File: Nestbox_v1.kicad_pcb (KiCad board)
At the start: 2 copper layers, 23 x 90 mm, 79 parts, among them P1 RX/TX, P2 TST/RST, P3 VDD/GND, P4 NFC_PWR_SEL, Q1 SFH 3605, SW1 SMD-BUTTON_2P-3.0X2.5X1.2+0.4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, U1 MSP430FR5969, U2 CR95HF, U3 TPS630250RNC, U4 RN2483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

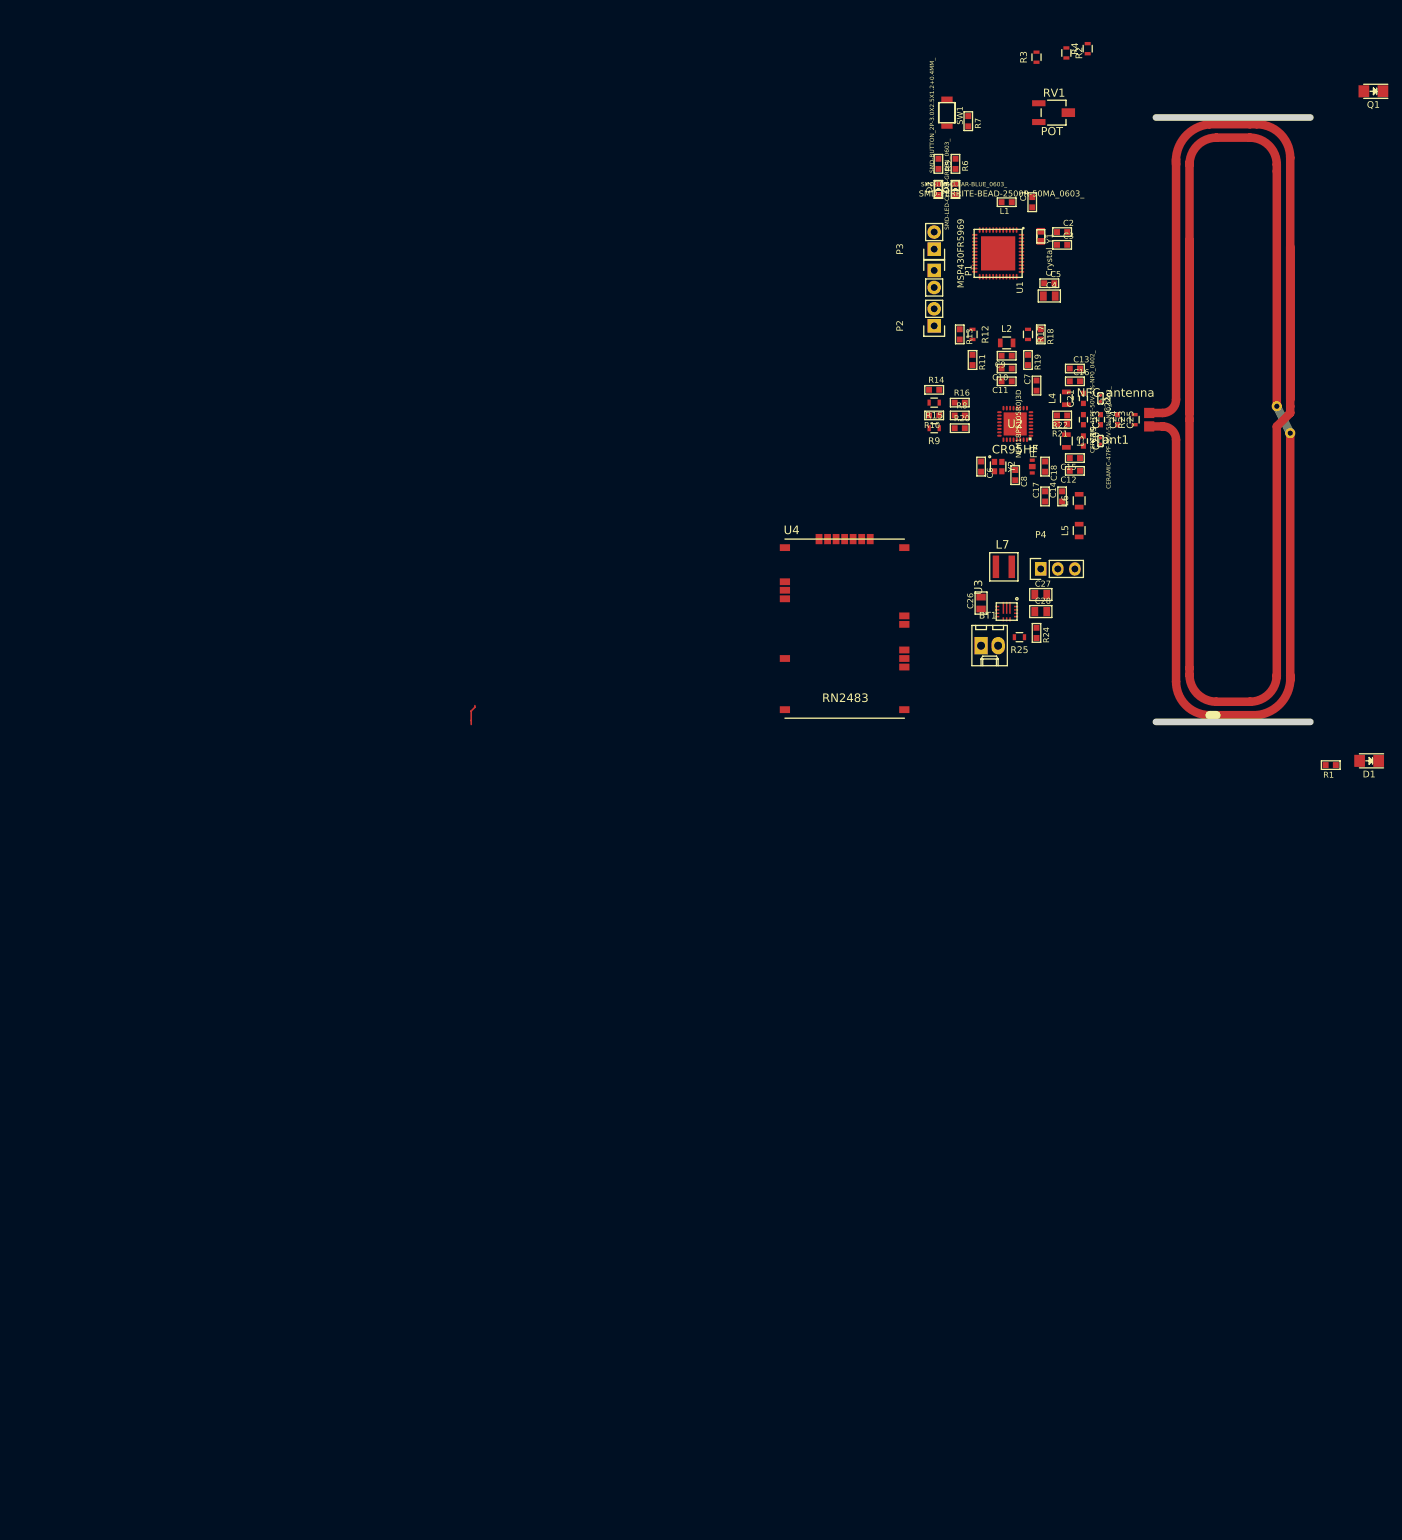
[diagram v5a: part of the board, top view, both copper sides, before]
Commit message: finished component placement incl. LoRa
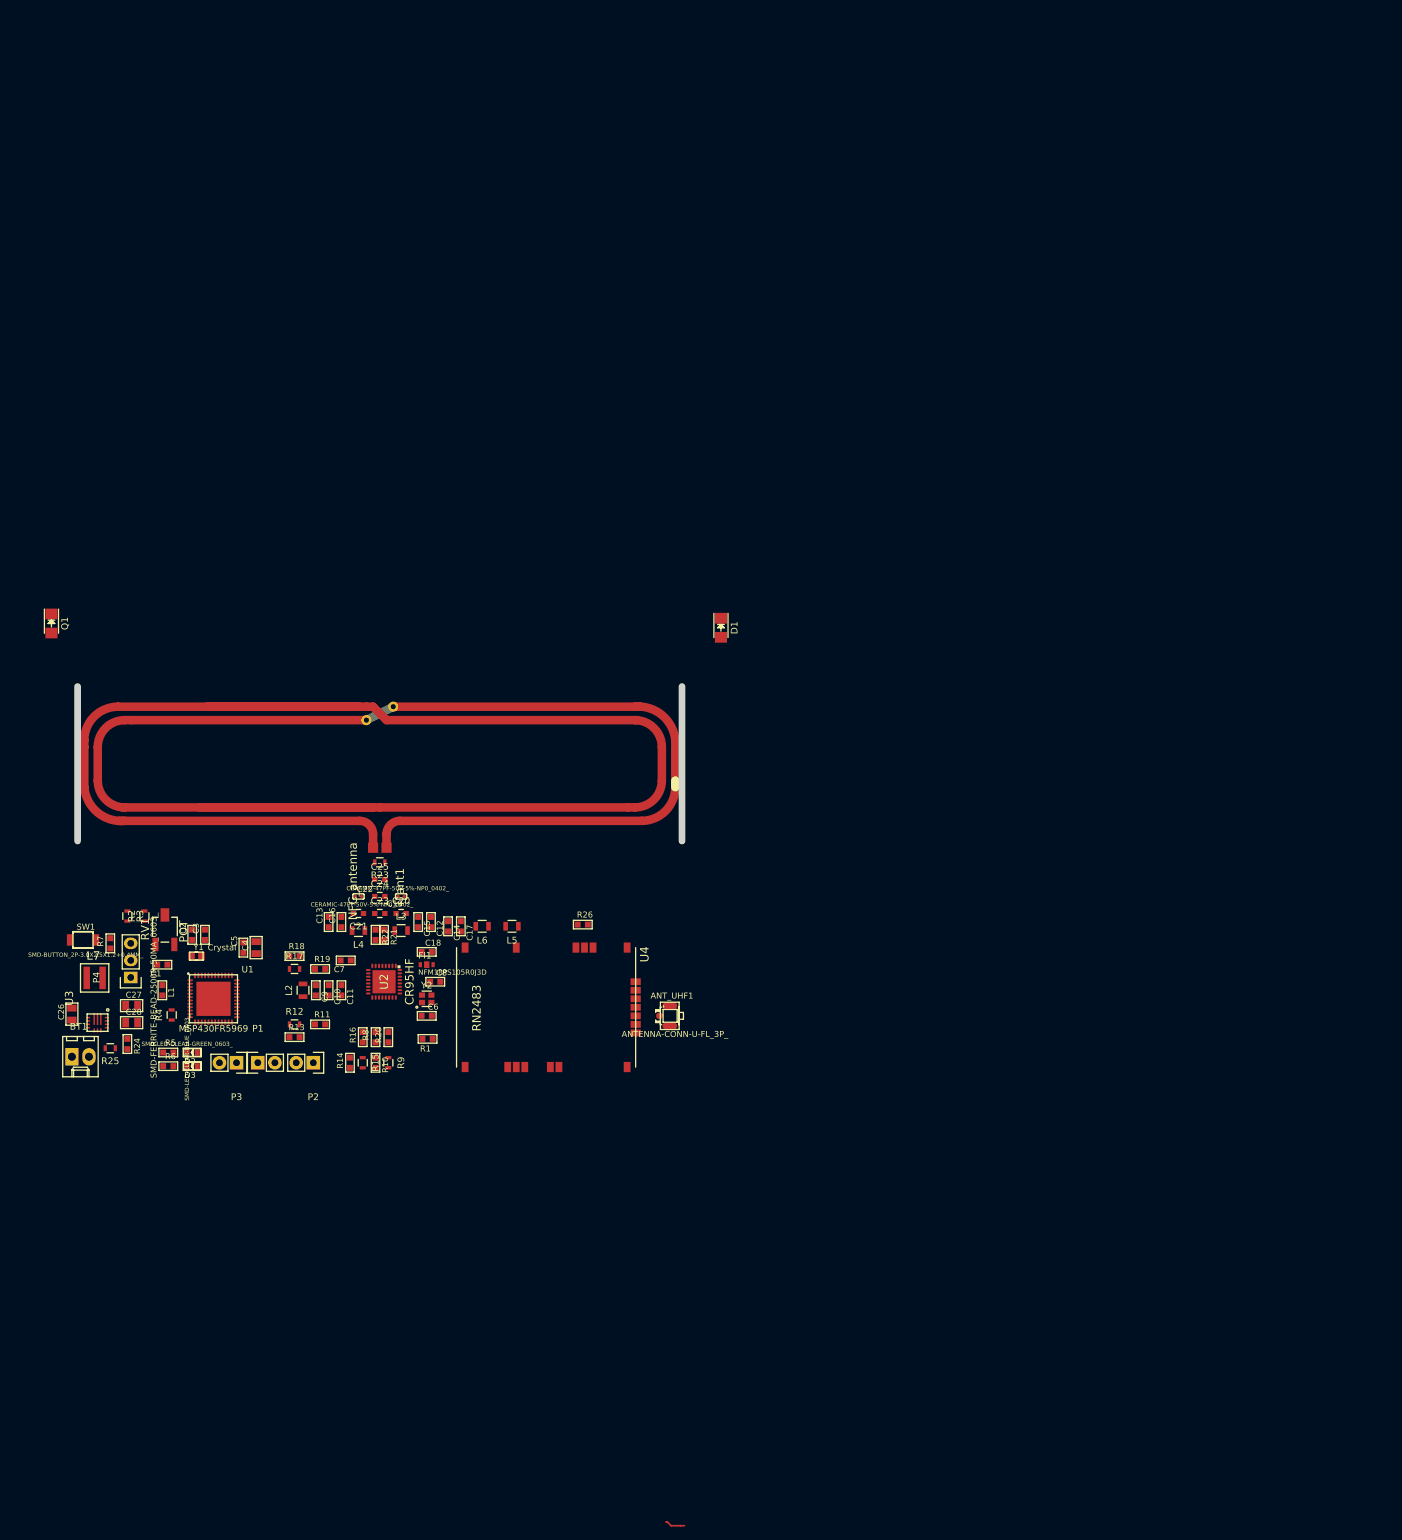
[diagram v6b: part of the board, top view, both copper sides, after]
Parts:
- added ANT_UHF1: ANTENNA-CONN-U-FL_3P_, SeeedOPL-Connector-2016:U-FL3P-SMD-2.6X2.6X1.0MM, F.Cu at (170.0, 120.9)
- added R26: SMD-RES-10K-1%-1_10W_0603_, SeeedOPL-Resistor-2016:R0603, F.Cu at (157.1, 107.4)
- moved Q1 212.2 mm to (77.9, 62.5), turned to 270 degrees
- moved R4 198.3 mm to (95.9, 120.8)
- moved R2 188.1 mm to (91.8, 106.1), turned to 90 degrees
- moved R3 186.2 mm to (89.2, 106.1), turned to 270 degrees
- moved RV1 179.8 mm to (94.8, 108.1), turned to 90 degrees
- moved R6 178.3 mm to (95.3, 128.4), turned to 270 degrees
- moved SW1 178.1 mm to (82.6, 109.6), turned to 0 degrees
- moved R7 177.0 mm to (86.7, 110.1), turned to 0 degrees
- moved R5 175.1 mm to (95.3, 126.4), turned to 270 degrees
- moved D3 173.1 mm to (98.9, 128.4), turned to 180 degrees
- moved C1 172.3 mm to (94.5, 113.3), turned to 270 degrees
- moved L1 172.0 mm to (94.5, 117.1), turned to 270 degrees
- moved D2 169.9 mm to (98.9, 126.4), turned to 180 degrees
- moved C2 166.5 mm to (98.9, 108.9), turned to 180 degrees
- moved Y1 165.2 mm to (99.5, 112.1), turned to 0 degrees
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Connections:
- U1 pad 12: (no net) -> Net-(U1-Pad12)
- U1 pad 13: (no net) -> Net-(U1-Pad13)
- U1 pad 14: (no net) -> Net-(U1-Pad14)
- U1 pad 15: (no net) -> Net-(U1-Pad15)
- U1 pad 19: (no net) -> Net-(U1-Pad19)
- U1 pad 2: (no net) -> Net-(U1-Pad2)
- U1 pad 28: (no net) -> Net-(U1-Pad28)
- U1 pad 3: (no net) -> Net-(U1-Pad3)
- U1 pad 33: (no net) -> Net-(U1-Pad33)
- U1 pad 34: (no net) -> Net-(U1-Pad34)
- U1 pad 35: (no net) -> LORA_RST_N
- U1 pad 38: (no net) -> Net-(U1-Pad38)
- U1 pad 39: (no net) -> Net-(U1-Pad39)
- U1 pad 4: (no net) -> Net-(U1-Pad4)
- U1 pad 40: (no net) -> Net-(U1-Pad40)
- U1 pad 42: (no net) -> Net-(U1-Pad42)
- U1 pad 43: (no net) -> Net-(U1-Pad43)
- U1 pad 5: (no net) -> Net-(U1-Pad5)
- U1 pad 6: (no net) -> Net-(U1-Pad6)
- U1 pad 7: (no net) -> Net-(U1-Pad7)
- U1 pad 8: (no net) -> Net-(U1-Pad8)
- U1 pad 9: (no net) -> Net-(U1-Pad9)
- U4 pad 23: (no net) -> Net-(ANT_UHF1-PadD)
- U4 pad 25: (no net) -> Net-(U4-Pad25)
- U4 pad 32: (no net) -> LORA_RST_N
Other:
- board size 23 x 90 mm -> 90 x 23 mm

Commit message: board outline
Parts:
- moved ANT_UHF1 24.3 mm to (190.8, 133.5)
- moved R26 24.0 mm to (177.4, 120.1)
- moved U4 23.5 mm to (158.3, 123.1)
- moved C14 23.4 mm to (157.3, 119.3)
- moved C17 23.4 mm to (159.2, 119.3)
- moved L5 23.4 mm to (166.8, 119.3)
- moved L6 23.4 mm to (162.4, 119.3)
- moved BT1 22.6 mm to (100.8, 138.0)
- moved C10 22.6 mm to (139.0, 128.1)
- moved C11 22.6 mm to (140.9, 128.1)
- moved C6 22.6 mm to (153.6, 131.9)
- moved C9 22.6 mm to (137.1, 128.1)
- moved FI1 22.6 mm to (153.6, 124.2)
- moved L2 22.6 mm to (135.2, 128.1)
- moved L3 22.6 mm to (149.8, 119.2)
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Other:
- board size 90 x 23 mm -> 100 x 91 mm

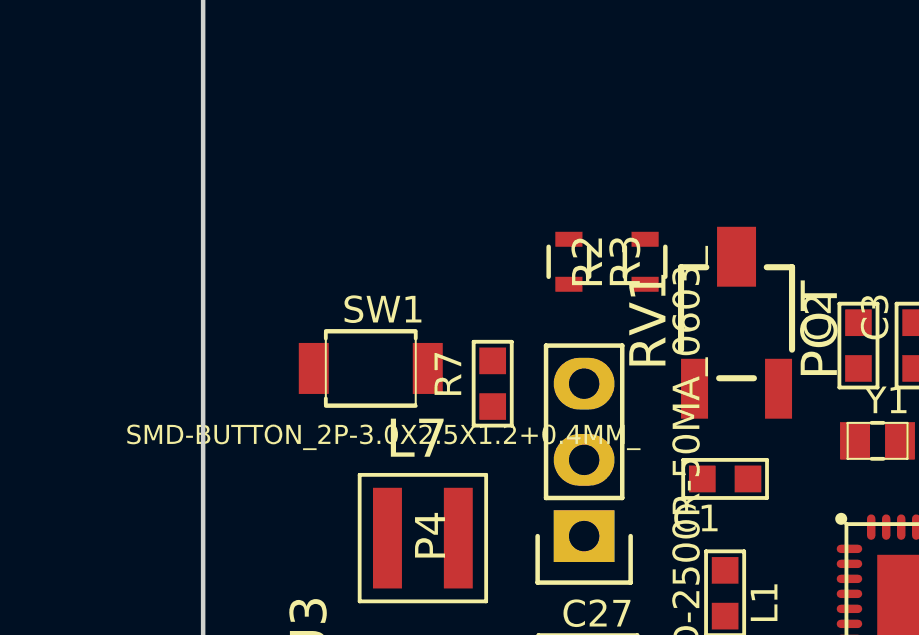
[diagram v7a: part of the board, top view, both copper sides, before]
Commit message: added additional connector for light barrier
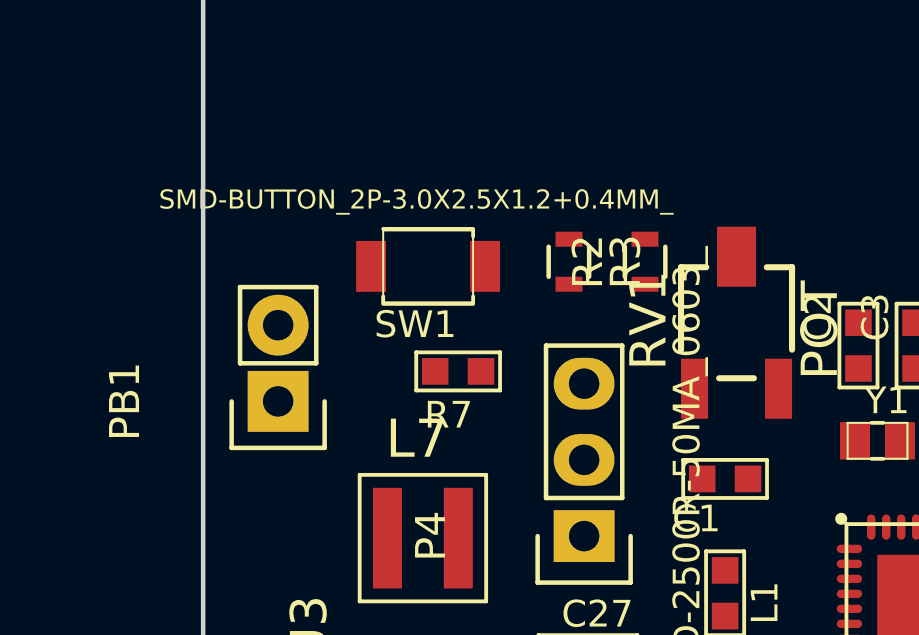
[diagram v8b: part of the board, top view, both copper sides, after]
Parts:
- added PB1: LIGHT_BARRIER2, Socket_Strips:Socket_Strip_Straight_1x02, F.Cu at (99.4, 121.7)
- moved SW1 3.90 mm to (104.4, 117.2), turned to 180 degrees
- moved R7 1.22 mm to (105.4, 120.7), turned to 90 degrees
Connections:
- U1 pad 12: Net-(U1-Pad12) -> (no net)
- U1 pad 13: Net-(U1-Pad13) -> (no net)
- U1 pad 14: Net-(U1-Pad14) -> (no net)
- U1 pad 15: Net-(U1-Pad15) -> (no net)
- U1 pad 19: Net-(U1-Pad19) -> (no net)
- U1 pad 28: Net-(U1-Pad28) -> (no net)
- U1 pad 3: Net-(U1-Pad3) -> (no net)
- U1 pad 33: Net-(U1-Pad33) -> (no net)
- U1 pad 34: Net-(U1-Pad34) -> (no net)
- U1 pad 38: Net-(U1-Pad38) -> (no net)
- U1 pad 39: Net-(U1-Pad39) -> (no net)
- U1 pad 4: Net-(U1-Pad4) -> (no net)
- U1 pad 40: Net-(U1-Pad40) -> (no net)
- U1 pad 42: Net-(U1-Pad42) -> (no net)
- U1 pad 43: Net-(U1-Pad43) -> (no net)
- U1 pad 5: Net-(U1-Pad5) -> (no net)
- U1 pad 6: Net-(U1-Pad6) -> (no net)
- U1 pad 7: Net-(U1-Pad7) -> (no net)
- U1 pad 8: Net-(U1-Pad8) -> (no net)
- U4 pad 25: Net-(U4-Pad25) -> (no net)
